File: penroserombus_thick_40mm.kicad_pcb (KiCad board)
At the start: 2 copper layers, 52.4 x 38 mm, 21 parts, among them J1 Conn_01x03_Female, J2 Conn_01x03_Female, J3 Conn_01x03_Male, J4 Conn_01x03_Male, M2.1 MountingHole_2.1mm, SW1 SW_DPDT_x2

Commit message: small tweaks to thick rhombus.
shifted letters and moved jumpers closer to switch
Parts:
- moved JP2 2.32 mm to (151.1, 99.0)
- moved JP1 2.04 mm to (144.6, 90.1)
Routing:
- net Net-(D1-Pad4): track 17.2 -> 13.0 mm
- net Net-(D4-Pad2): track 25.2 -> 21.7 mm
- net Net-(D3-Pad2): track 21.4 -> 18.1 mm
- net Net-(D2-Pad4): track 17.0 -> 15.2 mm
- net VCC: track 102.8 -> 101.4 mm
- net GND: vias 9 -> 10
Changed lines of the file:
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@@
     (thickness 1.6)
     (drawings 32)
-    (tracks 90)
+    (tracks 88)
     (zones 0)
     (modules 21)
@@
   )
   (module Jumper:SolderJumper-3_P1.3mm_Open_RoundedPad1.0x1.5mm (layer F.Cu)
-    (at 142.621 89.662 36)
+    (at 144.617278 90.095921 36)
     (descr "SMD Solder 3-pad Jumper, 1x1.5mm rounded Pads, 0.3mm gap, open")
     (tags "solder jumper open")
@@
   )
   (module Jumper:SolderJumper-3_P1.3mm_Open_RoundedPad1.0x1.5mm (layer F.Cu)
-    (at 150.622 101.219 36)
+    (at 151.13 98.9584 36)
     (descr "SMD Solder 3-pad Jumper, 1x1.5mm rounded Pads, 0.3mm gap, open")
     (tags "solder jumper open")
     (attr virtual)
-    (fp_text reference JP2 (at 0 -1.8 36) (layer F.SilkS)
+    (fp_text reference JP2 (at 0.215626 1.820656 36) (layer F.SilkS)
       (effects (font (size 1 1) (thickness 0.15)))
     )
@@
   (gr_arc (start 120.85162 114.02826) (end 150.90162 114.02826) (angle -72) (layer Dwgs.User) (width 0.2))
   (gr_arc (start 120.85162 114.02826) (end 149.85162 114.02826) (angle -72) (layer Dwgs.User) (width 0.2))
-  (gr_text A (at 162.052 101.854 162) (layer F.SilkS)
+  (gr_text A (at 161.8742 102.7938 162) (layer F.SilkS)
     (effects (font (size 2 2) (thickness 0.5)))
   )
-  (gr_text T (at 145.288 78.486 90) (layer F.SilkS)
+  (gr_text T (at 144.1958 78.4098 90) (layer F.SilkS)
     (effects (font (size 2 2) (thickness 0.5)))
   )
@@
   (segment (start 145.288 83.1635) (end 147.581513 83.125141) (width 1) (layer F.Cu) (net 1))
   (segment (start 139.446 103.6105) (end 136.662962 103.6105) (width 1) (layer F.Cu) (net 1))
-  (segment (start 158.380327 89.713953) (end 152.991516 84.325142) (width 1) (layer F.Cu) (net 1))
   (segment (start 136.968996 94.245872) (end 134.047512 97.167356) (width 1) (layer F.Cu) (net 1))
   (segment (start 128.624698 98.195356) (end 133.252279 99.374395) (width 1) (layer F.Cu) (net 1))
@@
   (segment (start 155.458843 97.167356) (end 158.380327 93.20141) (width 1) (layer F.Cu) (net 1))
   (segment (start 145.288 83.1635) (end 143.2345 83.1635) (width 1) (layer F.Cu) (net 1))
-  (segment (start 136.968996 94.245872) (end 138.792008 88.627008) (width 1) (layer F.Cu) (net 1))
-  (segment (start 138.792008 88.627008) (end 143.2345 83.1635) (width 1) (layer F.Cu) (net 1))
   (segment (start 138.31162 111.52826) (end 136.662962 103.6105) (width 1) (layer F.Cu) (net 1))
-  (segment (start 133.252279 99.374395) (end 134.142017 101.950983) (width 1) (layer F.Cu) (net 1))
-  (segment (start 134.142017 101.950983) (end 136.662962 103.6105) (width 1) (layer F.Cu) (net 1))
   (segment (start 161.163 92.202) (end 158.380327 91.324327) (width 1) (layer F.Cu) (net 1))
-  (segment (start 158.380327 91.324327) (end 158.380327 89.713953) (width 1) (layer F.Cu) (net 1))
   (segment (start 158.380327 93.20141) (end 158.380327 91.324327) (width 1) (layer F.Cu) (net 1))
   (segment (start 141.582407 103.689119) (end 144.907 105.283) (width 1) (layer F.Cu) (net 1))
-  (segment (start 144.907 105.283) (end 149.098 105.283) (width 1) (layer F.Cu) (net 1))
-  (segment (start 149.098 105.283) (end 153.67 101.981) (width 1) (layer F.Cu) (net 1))
-  (segment (start 153.67 101.981) (end 154.715279 99.247395) (width 1) (layer F.Cu) (net 1))
   (segment (start 149.403635 78.486676) (end 147.581513 83.125141) (width 1) (layer F.Cu) (net 1))
   (segment (start 163.476732 97.856635) (end 161.75228 95.3008) (width 1) (layer F.Cu) (net 1))
   (segment (start 161.75228 95.3008) (end 161.754736 92.405284) (width 1) (layer F.Cu) (net 1))
   (segment (start 161.754736 92.405284) (end 161.163 92.202) (width 1) (layer F.Cu) (net 1))
+  (segment (start 154.715279 99.247395) (end 147.5486 105.283) (width 1) (layer F.Cu) (net 1))
+  (segment (start 144.907 105.283) (end 147.5486 105.283) (width 1) (layer F.Cu) (net 1))
+  (segment (start 143.2345 83.1635) (end 137.815129 91.637929) (width 1) (layer F.Cu) (net 1))
+  (segment (start 136.968996 94.245872) (end 137.815129 91.637929) (width 1) (layer F.Cu) (net 1))
+  (segment (start 158.380327 91.324327) (end 152.991516 84.325142) (width 1) (layer F.Cu) (net 1))
+  (segment (start 136.662962 103.6105) (end 133.855151 101.120249) (width 1) (layer F.Cu) (net 1))
+  (segment (start 133.252279 99.374395) (end 133.855151 101.120249) (width 1) (layer F.Cu) (net 1))
   (via (at 141.224 105.41) (size 0.8) (drill 0.4) (layers F.Cu B.Cu) (net 2))
   (via (at 138.176 94.996) (size 0.8) (drill 0.4) (layers F.Cu B.Cu) (net 2))
@@
   (segment (start 165.75532 95.92564) (end 164.62248 99.49434) (width 0.25) (layer F.Cu) (net 2))
   (segment (start 164.62248 99.49434) (end 161.94532 98.74758) (width 0.25) (layer F.Cu) (net 2))
+  (via (at 148.0058 101.6) (size 0.8) (drill 0.4) (layers F.Cu B.Cu) (net 2))
   (segment (start 162.691829 100.272318) (end 158.502224 98.156211) (width 0.25) (layer F.Cu) (net 3))
-  (segment (start 149.488493 96.773473) (end 150.622 101.219) (width 0.25) (layer F.Cu) (net 4))
-  (segment (start 153.673275 95.80693) (end 156.973026 92.507179) (width 0.25) (layer F.Cu) (net 4))
-  (segment (start 151.15894 101.75594) (end 151.887377 101.75594) (width 0.25) (layer F.Cu) (net 4))
-  (segment (start 150.622 101.219) (end 151.15894 101.75594) (width 0.25) (layer F.Cu) (net 4))
-  (segment (start 151.887377 101.75594) (end 152.983659 100.659659) (width 0.25) (layer F.Cu) (net 4))
-  (segment (start 153.673275 95.80693) (end 152.983659 100.659659) (width 0.25) (layer F.Cu) (net 4))
+  (segment (start 149.488493 96.773473) (end 151.13 98.9584) (width 0.25) (layer F.Cu) (net 4))
+  (segment (start 151.13 98.9584) (end 152.5016 99.7204) (width 0.25) (layer F.Cu) (net 4))
+  (segment (start 152.5016 99.7204) (end 153.416 99.0346) (width 0.25) (layer F.Cu) (net 4))
+  (segment (start 153.416 99.0346) (end 154.432 96.012) (width 0.25) (layer F.Cu) (net 4))
+  (segment (start 154.432 96.012) (end 156.973026 92.507179) (width 0.25) (layer F.Cu) (net 4))
   (segment (start 146.167507 92.202527) (end 147.30998 93.345) (width 0.25) (layer F.Cu) (net 5) (status 10))
   (segment (start 147.30998 93.345) (end 147.30998 96.00198) (width 0.25) (layer F.Cu) (net 5))
-  (segment (start 142.621 89.662) (end 146.167507 92.202527) (width 0.25) (layer F.Cu) (net 5))
   (segment (start 146.122891 103.329603) (end 146.122891 97.189069) (width 0.25) (layer F.Cu) (net 5))
   (segment (start 146.122891 97.189069) (end 147.30998 96.00198) (width 0.25) (layer F.Cu) (net 5))
   (segment (start 146.482407 103.689119) (end 146.122891 103.329603) (width 0.25) (layer F.Cu) (net 5))
+  (segment (start 144.617278 90.095921) (end 146.167507 92.202527) (width 0.25) (layer F.Cu) (net 5))
   (segment (start 139.676619 112.291381) (end 139.676619 108.794907) (width 0.25) (layer F.Cu) (net 6))
   (segment (start 139.676619 108.794907) (end 141.582407 106.889119) (width 0.25) (layer F.Cu) (net 6))
@@
   (segment (start 147.796293 91.12682) (end 147.796293 97.912594) (width 0.25) (layer F.Cu) (net 7) (status 30))
   (segment (start 147.796293 97.912594) (end 147.465951 98.242936) (width 0.25) (layer F.Cu) (net 7) (status 30))
-  (segment (start 143.672722 88.897879) (end 148.190049 90.733064) (width 0.25) (layer F.Cu) (net 7))
-  (segment (start 149.570278 101.983121) (end 147.465951 98.242936) (width 0.25) (layer F.Cu) (net 7))
   (segment (start 147.581513 86.325141) (end 148.190049 90.733064) (width 0.25) (layer F.Cu) (net 7))
+  (segment (start 145.669 89.3318) (end 148.190049 90.733064) (width 0.25) (layer F.Cu) (net 7))
+  (segment (start 147.465951 98.242936) (end 150.078278 99.722521) (width 0.25) (layer F.Cu) (net 7))
   (segment (start 152.037299 82.680927) (end 152.481513 83.125141) (width 0.25) (layer F.Cu) (net 8))
   (segment (start 152.481513 83.125141) (end 150.622 79.629) (width 0.25) (layer F.Cu) (net 8))
@@
   (segment (start 144.144964 93.67199) (end 146.304 94.234) (width 0.25) (layer F.Cu) (net 10) (status 10))
   (segment (start 146.304 94.234) (end 148.717 94.742) (width 0.25) (layer B.Cu) (net 10))
-  (segment (start 141.569278 90.426121) (end 144.144964 93.67199) (width 0.25) (layer F.Cu) (net 10))
-  (segment (start 151.511036 95.30401) (end 151.673722 100.454879) (width 0.25) (layer F.Cu) (net 10))
   (segment (start 137.090893 98.156211) (end 144.144964 93.67199) (width 0.25) (layer F.Cu) (net 10))
+  (segment (start 143.565556 90.860042) (end 144.144964 93.67199) (width 0.25) (layer F.Cu) (net 10))
+  (segment (start 151.511036 95.30401) (end 152.181722 98.194279) (width 0.25) (layer F.Cu) (net 10))
   (zone (net 2) (net_name GND) (layer F.Cu) (hatch edge 0.508)
     (connect_pads (clearance 0.508))

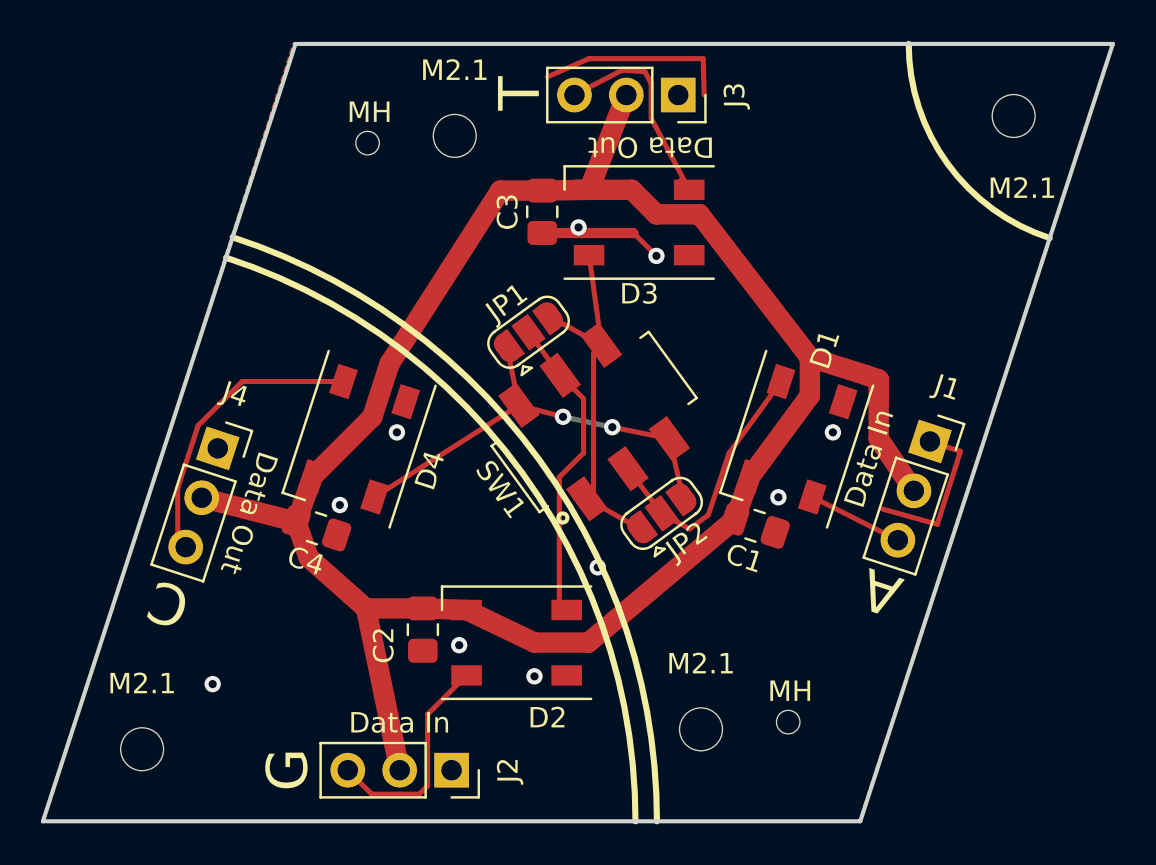
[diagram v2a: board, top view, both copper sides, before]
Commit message: increased mounting hole size to M3
increased mounting hole size to M3 to accomidate plastic adhesive mounting hole standoffs. makes the silkscreen a bit cramped and the VCC   route a bit long, but maybe I will make the top pour VCC instead of ground later idk.
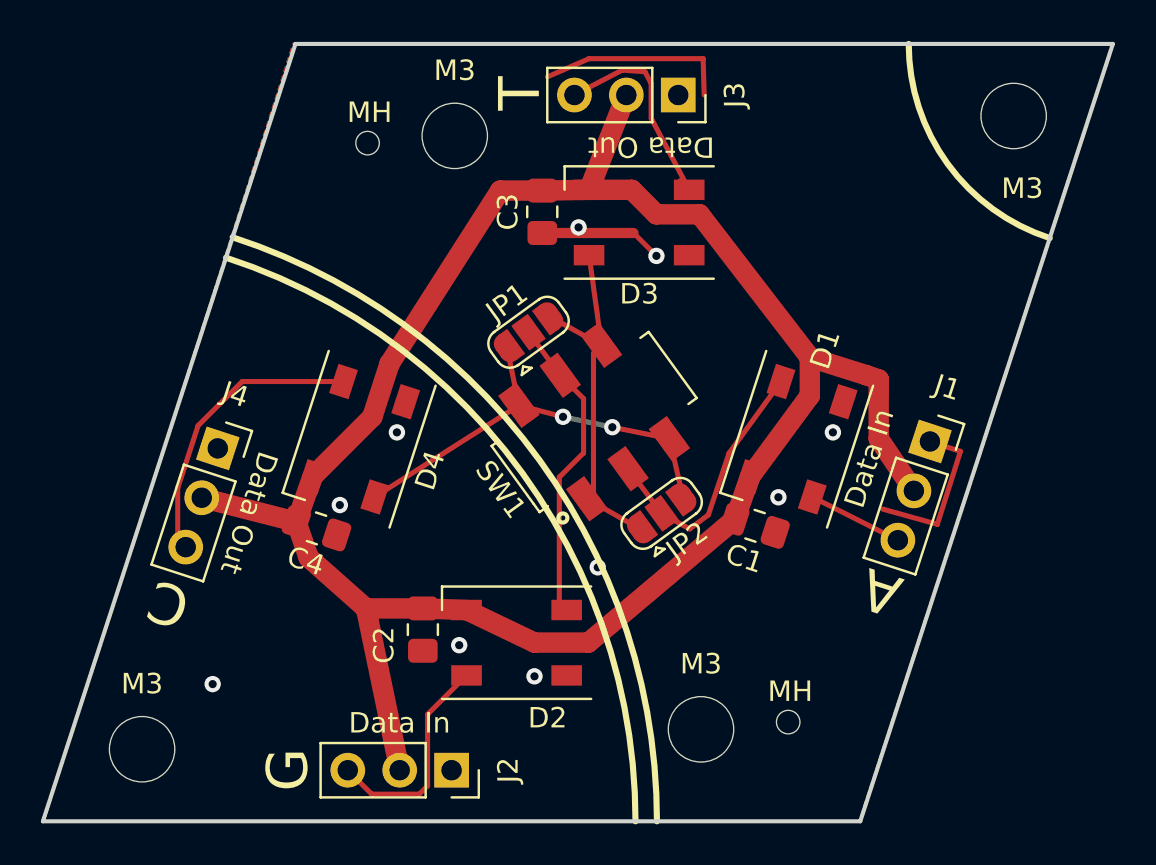
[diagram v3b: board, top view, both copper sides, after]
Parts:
- removed M2.1 (x3): MountingHole_2.1mm, MountingHole:MountingHole_2.1mm
- added M3: MountingHole_3.2mm_M3_ISO7380, MountingHole:MountingHole_3.2mm_M3_ISO7380, F.Cu at (153.1, 109.5)
- added M3: MountingHole_3.2mm_M3_ISO7380, MountingHole:MountingHole_3.2mm_M3_ISO7380, F.Cu at (141.0, 80.5)
- added M3: MountingHole_3.2mm_M3_ISO7380, MountingHole:MountingHole_3.2mm_M3_ISO7380, F.Cu at (168.4, 79.5)
- M3: renamed from M2.1; value MountingHole_2.1mm -> MountingHole_3.2mm_M3_ISO7380; footprint MountingHole:MountingHole_2.1mm -> MountingHole:MountingHole_3.2mm_M3_ISO7380
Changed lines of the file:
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@@
-(kicad_pcb (version 20171130) (host pcbnew 5.1.8)
+(kicad_pcb (version 20171130) (host pcbnew 5.1.9)
   (general
     (thickness 1.6)
@@
     (add_net VCC)
   )
-  (module MountingHole:MountingHole_2.1mm (layer F.Cu)
+  (module MountingHole:MountingHole_3.2mm_M3_ISO7380 (layer F.Cu)
+    (at 125.705721 110.501549)
+    (descr "Mounting Hole 3.2mm, no annular, M3, ISO7380")
+    (tags "mounting hole 3.2mm no annular m3 iso7380")
+    (attr virtual)
+    (fp_text reference M3 (at 0 -3.2) (layer F.SilkS)
+      (effects (font (size 1 1) (thickness 0.15)))
+    )
+    (fp_text value MountingHole_3.2mm_M3_ISO7380 (at 0 3.2) (layer F.Fab)
+      (effects (font (size 1 1) (thickness 0.15)))
+    )
+    (fp_circle (center 0 0) (end 3.1 0) (layer F.CrtYd) (width 0.05))
+    (fp_circle (center 0 0) (end 2.85 0) (layer Cmts.User) (width 0.15))
+    (fp_text user %R (at 0.3 0) (layer F.Fab)
+      (effects (font (size 1 1) (thickness 0.15)))
+    )
+    (pad 1 np_thru_hole circle (at 0 0) (size 3.2 3.2) (drill 3.2) (layers *.Cu *.Mask))
+  )
+  (module MountingHole:MountingHole_3.2mm_M3_ISO7380 (layer F.Cu)
+    (at 153.057392 109.528261)
+    (descr "Mounting Hole 3.2mm, no annular, M3, ISO7380")
+    (tags "mounting hole 3.2mm no annular m3 iso7380")
+    (attr virtual)
+    (fp_text reference M3 (at 0 -3.2) (layer F.SilkS)
+      (effects (font (size 1 1) (thickness 0.15)))
+    )
+    (fp_text value MountingHole_3.2mm_M3_ISO7380 (at 0 3.2) (layer F.Fab)
+      (effects (font (size 1 1) (thickness 0.15)))
+    )
+    (fp_circle (center 0 0) (end 3.1 0) (layer F.CrtYd) (width 0.05))
+    (fp_circle (center 0 0) (end 2.85 0) (layer Cmts.User) (width 0.15))
+    (fp_text user %R (at 0.3 0) (layer F.Fab)
+      (effects (font (size 1 1) (thickness 0.15)))
+    )
+    (pad 1 np_thru_hole circle (at 0 0) (size 3.2 3.2) (drill 3.2) (layers *.Cu *.Mask))
+  )
+  (module MountingHole:MountingHole_3.2mm_M3_ISO7380 (layer F.Cu)
     (at 141.006528 80.485999)
-    (descr "Mounting Hole 2.1mm, no annular")
-    (tags "mounting hole 2.1mm no annular")
-    (attr virtual)
-    (fp_text reference M2.1 (at 0 -3.2) (layer F.SilkS)
-      (effects (font (size 1 1) (thickness 0.15)))
-    )
-    (fp_text value MountingHole_2.1mm (at 0 3.2) (layer F.Fab)
-      (effects (font (size 1 1) (thickness 0.15)))
-    )
-    (fp_circle (center 0 0) (end 2.1 0) (layer Cmts.User) (width 0.15))
-    (fp_circle (center 0 0) (end 2.35 0) (layer F.CrtYd) (width 0.05))
-    (fp_text user %R (at 0.3 0) (layer F.Fab)
-      (effects (font (size 1 1) (thickness 0.15)))
-    )
-    (pad "" np_thru_hole circle (at 0 0) (size 2.1 2.1) (drill 2.1) (layers *.Cu *.Mask))
-  )
-  (module MountingHole:MountingHole_2.1mm (layer F.Cu)
+    (descr "Mounting Hole 3.2mm, no annular, M3, ISO7380")
+    (tags "mounting hole 3.2mm no annular m3 iso7380")
+    (attr virtual)
+    (fp_text reference M3 (at 0 -3.2) (layer F.SilkS)
+      (effects (font (size 1 1) (thickness 0.15)))
+    )
+    (fp_text value MountingHole_3.2mm_M3_ISO7380 (at 0 3.2) (layer F.Fab)
+      (effects (font (size 1 1) (thickness 0.15)))
+    )
+    (fp_circle (center 0 0) (end 3.1 0) (layer F.CrtYd) (width 0.05))
+    (fp_circle (center 0 0) (end 2.85 0) (layer Cmts.User) (width 0.15))
+    (fp_text user %R (at 0.3 0) (layer F.Fab)
+      (effects (font (size 1 1) (thickness 0.15)))
+    )
+    (pad 1 np_thru_hole circle (at 0 0) (size 3.2 3.2) (drill 3.2) (layers *.Cu *.Mask))
+  )
+  (module MountingHole:MountingHole_3.2mm_M3_ISO7380 (layer F.Cu)
     (at 168.358198 79.512711)
-    (descr "Mounting Hole 2.1mm, no annular")
-    (tags "mounting hole 2.1mm no annular")
-    (attr virtual)
-    (fp_text reference M2.1 (at 0.424802 3.545289) (layer F.SilkS)
-      (effects (font (size 1 1) (thickness 0.15)))
-    )
-    (fp_text value MountingHole_2.1mm (at 0 3.2) (layer F.Fab)
-      (effects (font (size 1 1) (thickness 0.15)))
-    )
-    (fp_circle (center 0 0) (end 2.1 0) (layer Cmts.User) (width 0.15))
-    (fp_circle (center 0 0) (end 2.35 0) (layer F.CrtYd) (width 0.05))
-    (fp_text user %R (at 0.3 0) (layer F.Fab)
-      (effects (font (size 1 1) (thickness 0.15)))
-    )
-    (pad "" np_thru_hole circle (at 0 0) (size 2.1 2.1) (drill 2.1) (layers *.Cu *.Mask))
-  )
-  (module MountingHole:MountingHole_2.1mm (layer F.Cu)
-    (at 153.057392 109.528261)
-    (descr "Mounting Hole 2.1mm, no annular")
-    (tags "mounting hole 2.1mm no annular")
-    (attr virtual)
-    (fp_text reference M2.1 (at 0 -3.2) (layer F.SilkS)
-      (effects (font (size 1 1) (thickness 0.15)))
-    )
-    (fp_text value MountingHole_2.1mm (at 0 3.2) (layer F.Fab)
-      (effects (font (size 1 1) (thickness 0.15)))
-    )
-    (fp_circle (center 0 0) (end 2.1 0) (layer Cmts.User) (width 0.15))
-    (fp_circle (center 0 0) (end 2.35 0) (layer F.CrtYd) (width 0.05))
-    (fp_text user %R (at 0.3 0) (layer F.Fab)
-      (effects (font (size 1 1) (thickness 0.15)))
-    )
-    (pad "" np_thru_hole circle (at 0 0) (size 2.1 2.1) (drill 2.1) (layers *.Cu *.Mask))
+    (descr "Mounting Hole 3.2mm, no annular, M3, ISO7380")
+    (tags "mounting hole 3.2mm no annular m3 iso7380")
+    (attr virtual)
+    (fp_text reference M3 (at 0.424802 3.545289) (layer F.SilkS)
+      (effects (font (size 1 1) (thickness 0.15)))
+    )
+    (fp_text value MountingHole_3.2mm_M3_ISO7380 (at 0 3.2) (layer F.Fab)
+      (effects (font (size 1 1) (thickness 0.15)))
+    )
+    (fp_circle (center 0 0) (end 3.1 0) (layer F.CrtYd) (width 0.05))
+    (fp_circle (center 0 0) (end 2.85 0) (layer Cmts.User) (width 0.15))
+    (fp_text user %R (at 0.3 0) (layer F.Fab)
+      (effects (font (size 1 1) (thickness 0.15)))
+    )
+    (pad 1 np_thru_hole circle (at 0 0) (size 3.2 3.2) (drill 3.2) (layers *.Cu *.Mask))
   )
   (module penroserombus:Pushpin_mountinghole (layer F.Cu)
@@
     (pad "" np_thru_hole circle (at 0 0) (size 1.15 1.15) (drill 1.15) (layers *.Cu *.Mask))
   )
-  (module MountingHole:MountingHole_2.1mm (layer F.Cu)
-    (at 125.705721 110.501549)
-    (descr "Mounting Hole 2.1mm, no annular")
-    (tags "mounting hole 2.1mm no annular")
-    (attr virtual)
-    (fp_text reference M2.1 (at 0 -3.2) (layer F.SilkS)
-      (effects (font (size 1 1) (thickness 0.15)))
-    )
-    (fp_text value MountingHole_2.1mm (at 0 3.2) (layer F.Fab)
-      (effects (font (size 1 1) (thickness 0.15)))
-    )
-    (fp_circle (center 0 0) (end 2.1 0) (layer Cmts.User) (width 0.15))
-    (fp_circle (center 0 0) (end 2.35 0) (layer F.CrtYd) (width 0.05))
-    (fp_text user %R (at 0.3 0) (layer F.Fab)
-      (effects (font (size 1 1) (thickness 0.15)))
-    )
-    (pad "" np_thru_hole circle (at 0 0) (size 2.1 2.1) (drill 2.1) (layers *.Cu *.Mask))
-  )
   (module Capacitor_SMD:C_0805_2012Metric_Pad1.18x1.45mm_HandSolder (layer F.Cu)
